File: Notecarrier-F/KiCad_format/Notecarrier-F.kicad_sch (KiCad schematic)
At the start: 0 parts

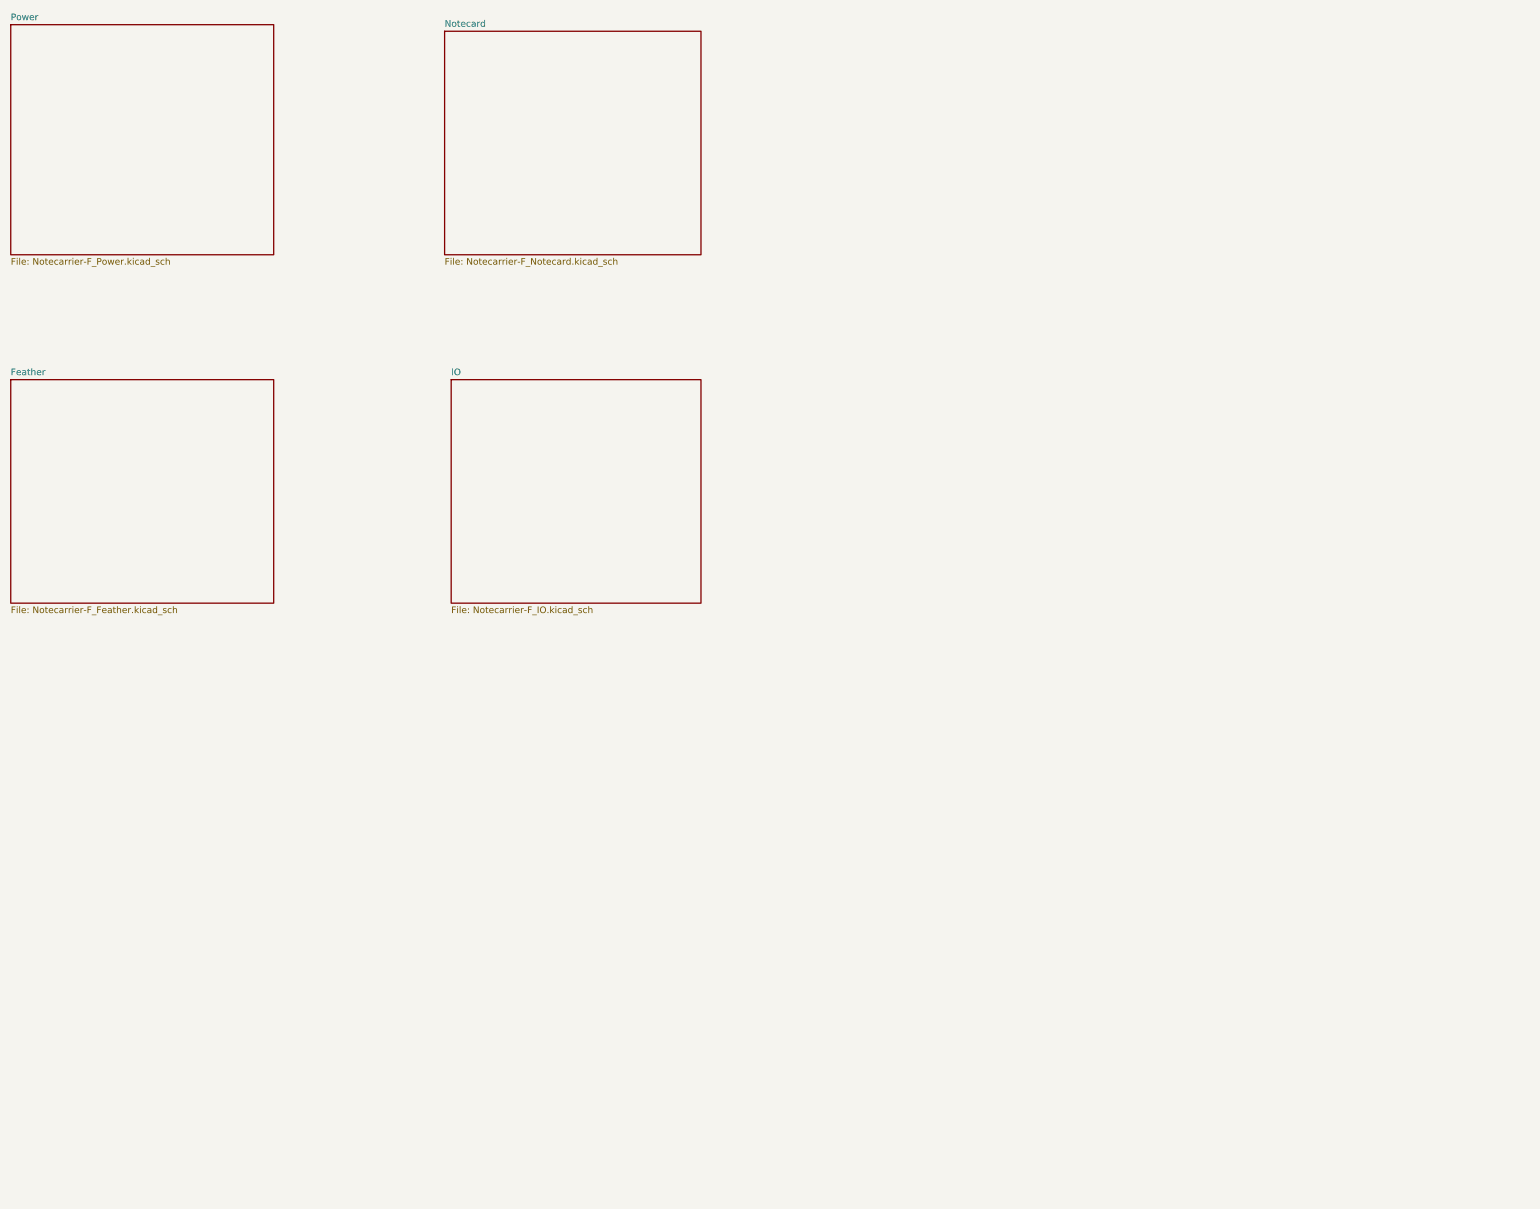
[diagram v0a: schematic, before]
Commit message: Port Notecarrier-F schematic and BOM.
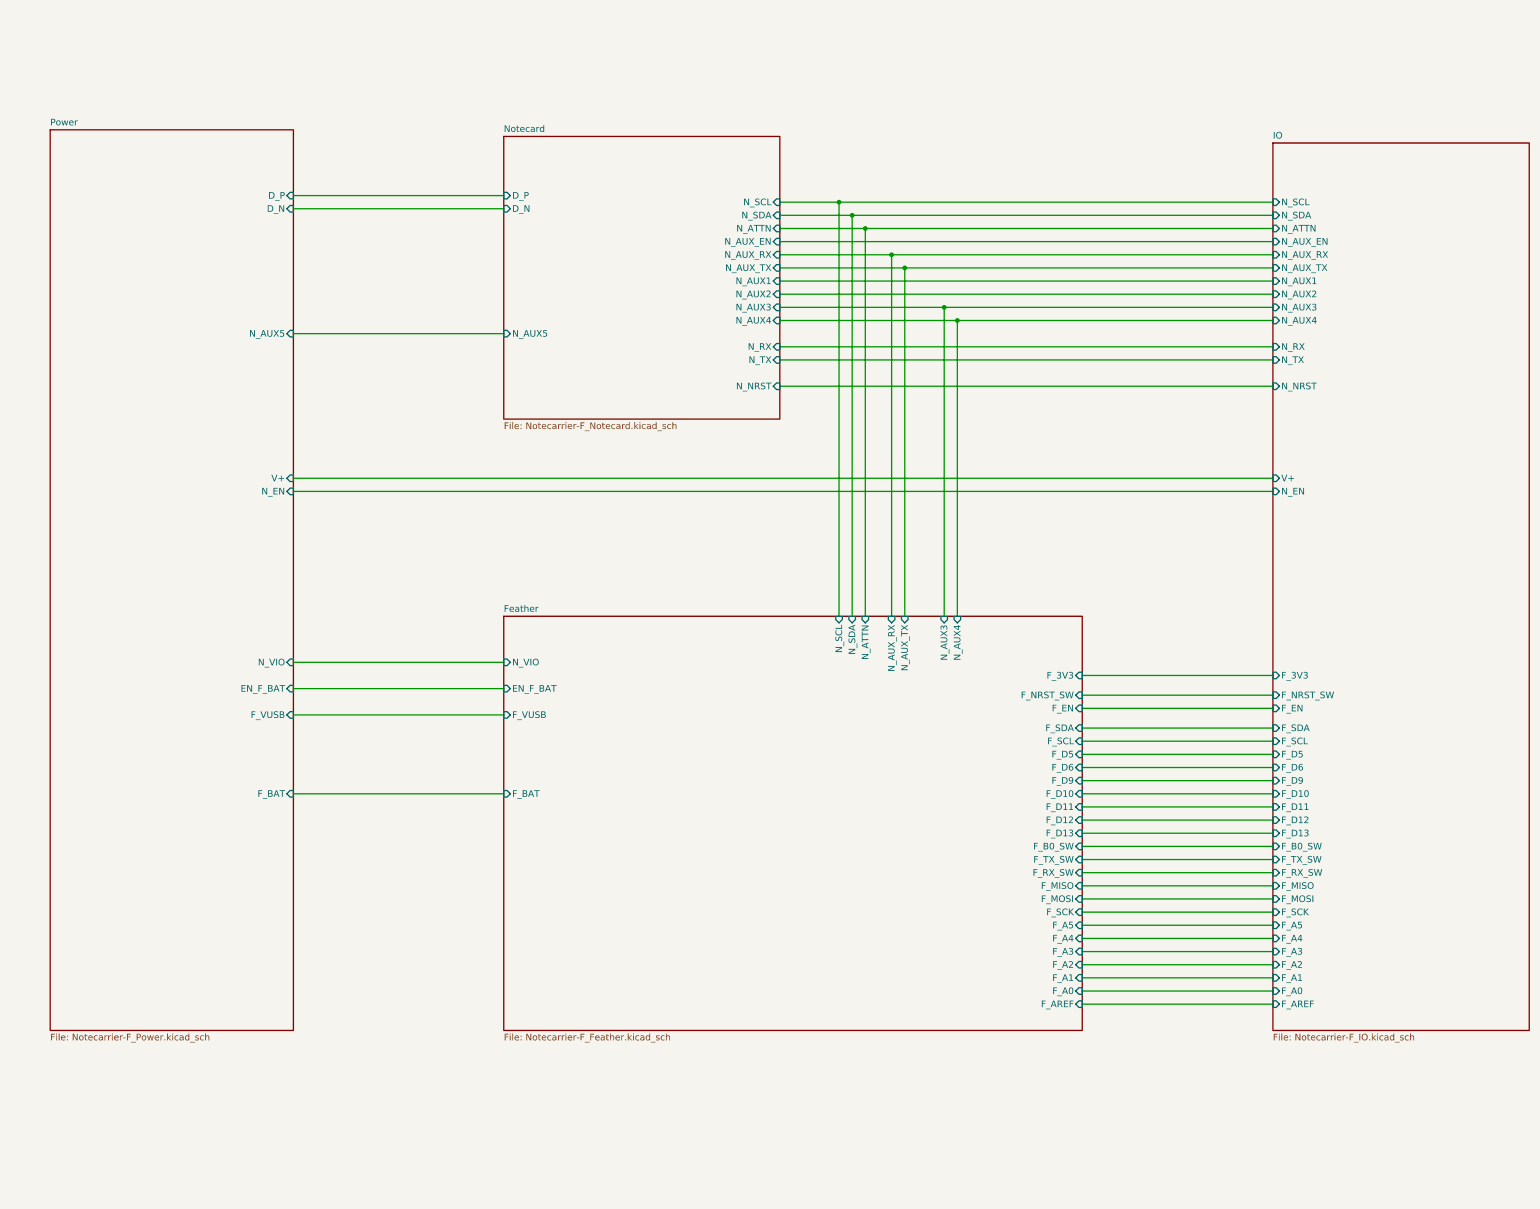
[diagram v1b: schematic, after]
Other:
- sheet Feather ports: added EN_F_BAT, F_3V3, F_A0, F_A1, F_A2, F_A3, F_A4, F_A5, F_AREF, F_B0_SW, F_BAT, F_D10, F_D11, F_D12, F_D13, F_D5, F_D6, F_D9, F_EN, F_MISO, F_MOSI, F_NRST_SW, F_RX_SW, F_SCK, F_SCL, F_SDA, F_TX_SW, F_VUSB, N_ATTN, N_AUX3, N_AUX4, N_AUX_RX, N_AUX_TX, N_SCL, N_SDA, N_VIO; removed none
- sheet IO ports: added F_3V3, F_A0, F_A1, F_A2, F_A3, F_A4, F_A5, F_AREF, F_B0_SW, F_D10, F_D11, F_D12, F_D13, F_D5, F_D6, F_D9, F_EN, F_MISO, F_MOSI, F_NRST_SW, F_RX_SW, F_SCK, F_SCL, F_SDA, F_TX_SW, N_ATTN, N_AUX1, N_AUX2, N_AUX3, N_AUX4, N_AUX_EN, N_AUX_RX, N_AUX_TX, N_EN, N_NRST, N_RX, N_SCL, N_SDA, N_TX, V+; removed none
- sheet Notecard ports: added D_N, D_P, N_ATTN, N_AUX1, N_AUX2, N_AUX3, N_AUX4, N_AUX5, N_AUX_EN, N_AUX_RX, N_AUX_TX, N_NRST, N_RX, N_SCL, N_SDA, N_TX; removed none
- sheet Power ports: added D_N, D_P, EN_F_BAT, F_BAT, F_VUSB, N_AUX5, N_EN, N_VIO, V+; removed none

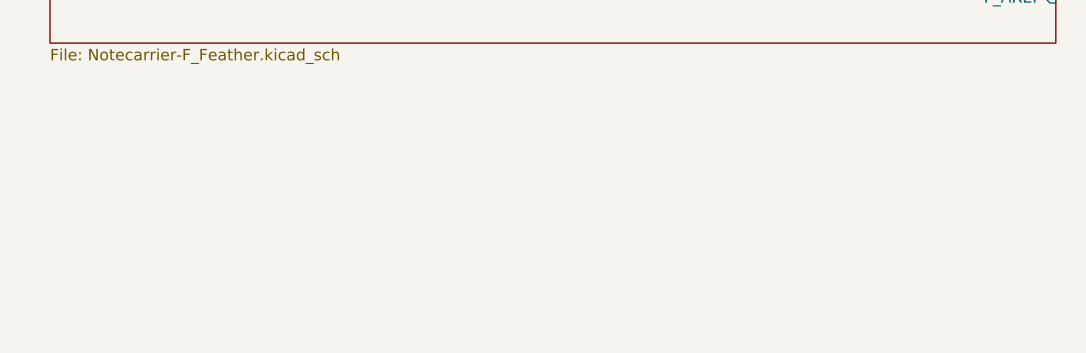
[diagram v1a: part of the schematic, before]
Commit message: Finish first pass PCB port.
Still need to go back and finalise top-level schematic sheet.
Next step is validation where there’s bound to be lots of copper rules to tweak.
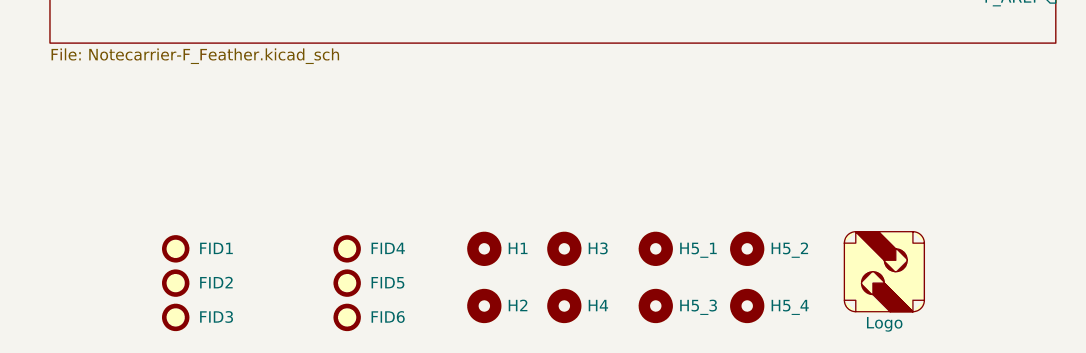
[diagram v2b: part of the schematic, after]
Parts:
- added FID1, FID2, FID3, FID4, FID5, FID6: TPS, blues-kicad-lib-pending:FIDUCIAL, symbol Mechanical:Fiducial
- added G1: Logo, blues-kicad-lib-pending:Logo_19.5x12.5, symbol blues-kicad-lib:Logo_Blues_Wireless
- added H1, H2, H3, H4: MountingHole, blues-kicad-lib-pending:MountingHole_3.3mm_no-courtyard, symbol Mechanical:MountingHole
- added H5_1, H5_2, H5_3, H5_4: MountingHole, blues-kicad-lib-pending:MountingHole_2.54mm_no-courtyard, symbol Mechanical:MountingHole

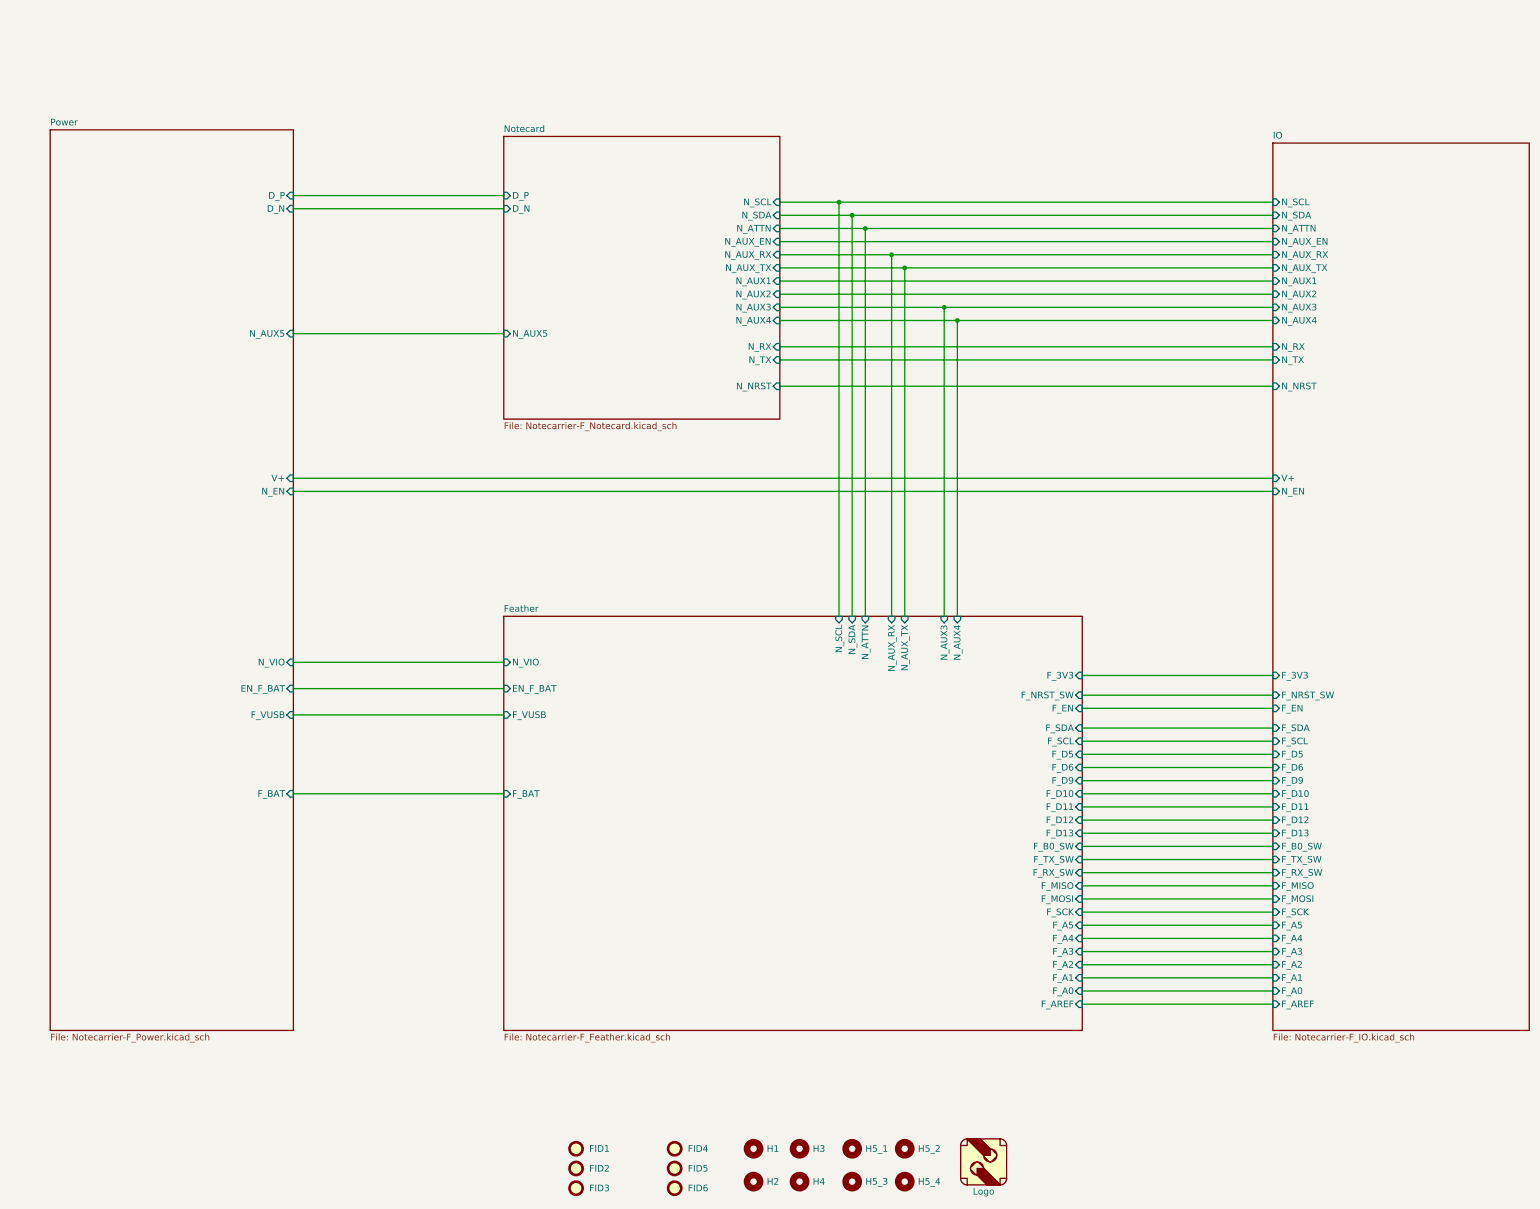
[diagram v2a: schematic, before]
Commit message: Apply first pass validation of Notecarrier-F port
Huge push to identify, solve, document and revalidate all the details revealed by the first run of the validation process. Validation is now acceptable and preparation can be made to release Rev A.
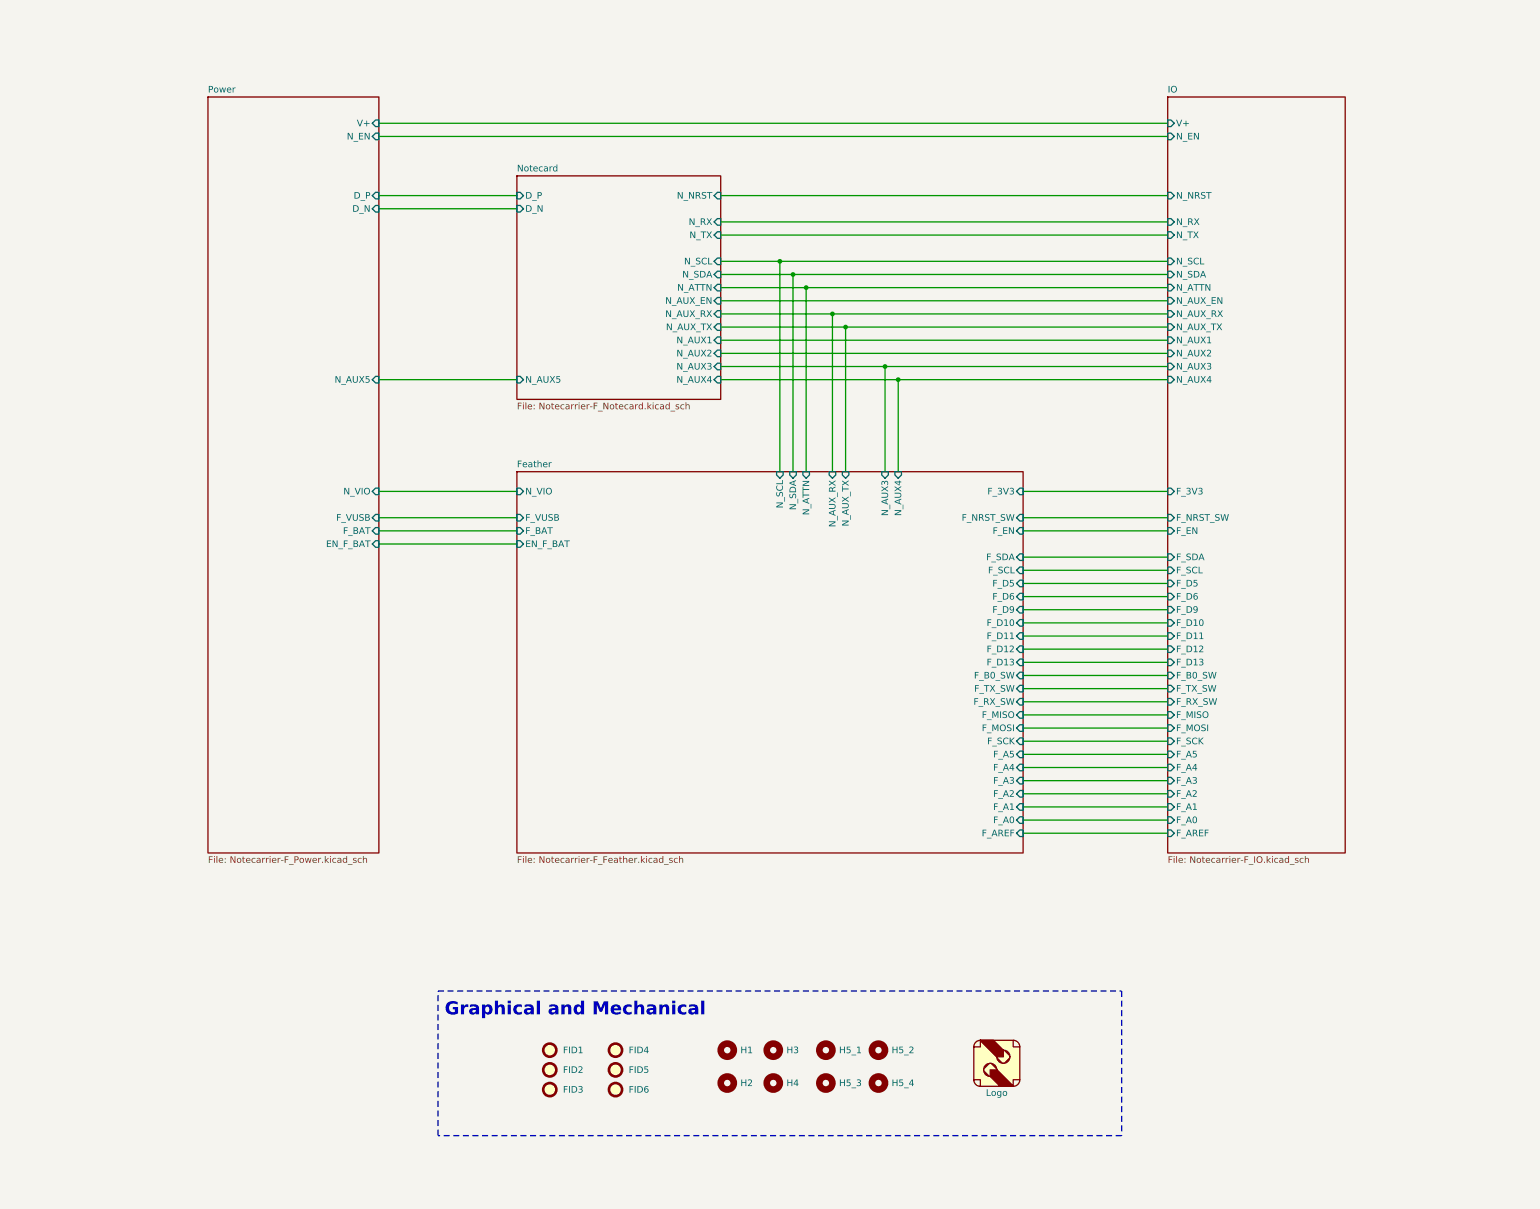
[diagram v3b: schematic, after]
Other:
- note added: "Graphical and Mechanical"
- moved on the sheet: FID1, FID2, FID3, FID4, FID5, FID6, H1, H2, H3, H4, H5_1, H5_2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
